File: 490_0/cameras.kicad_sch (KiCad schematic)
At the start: 2 parts, among them J1 2 lane camera interface, J2 4 lane camera interface

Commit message: Update cameras.kicad_sch
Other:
- note added: "WIDE ANGLE VERSION Horizontal field of view: 102 degrees Vertical field of view: 67 degrees"

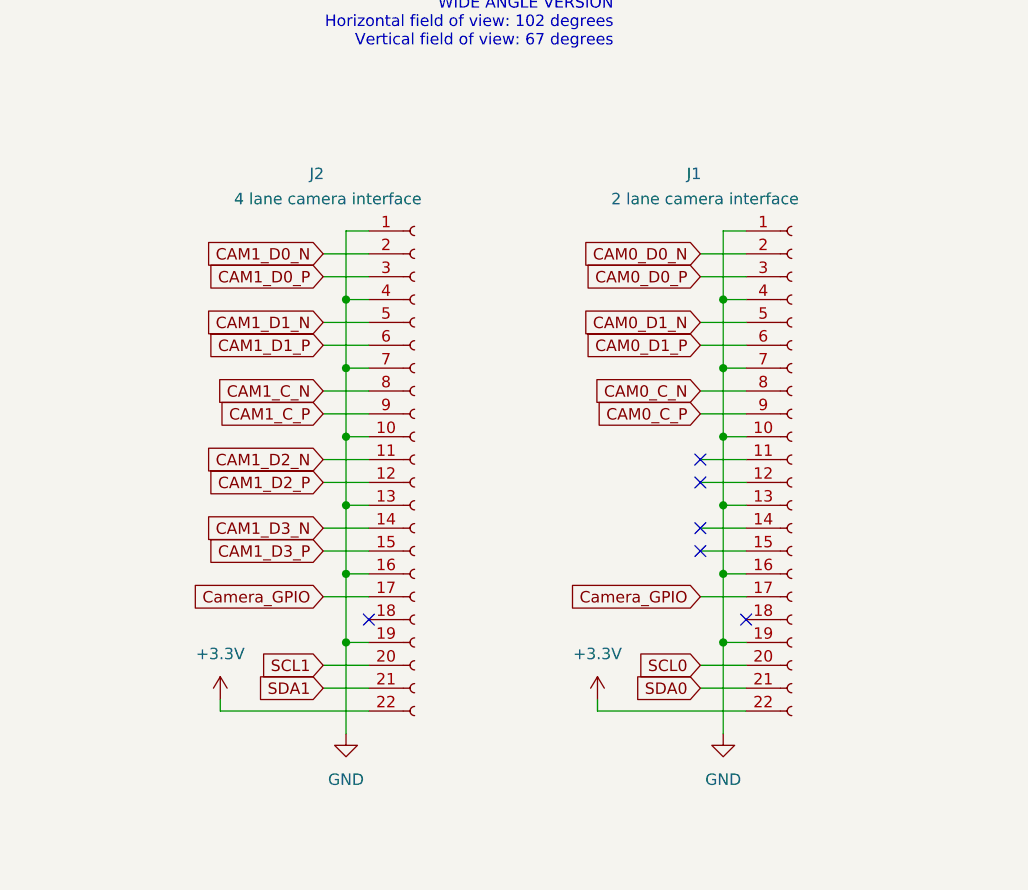
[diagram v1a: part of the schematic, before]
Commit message: Minor updates + USB 2.0
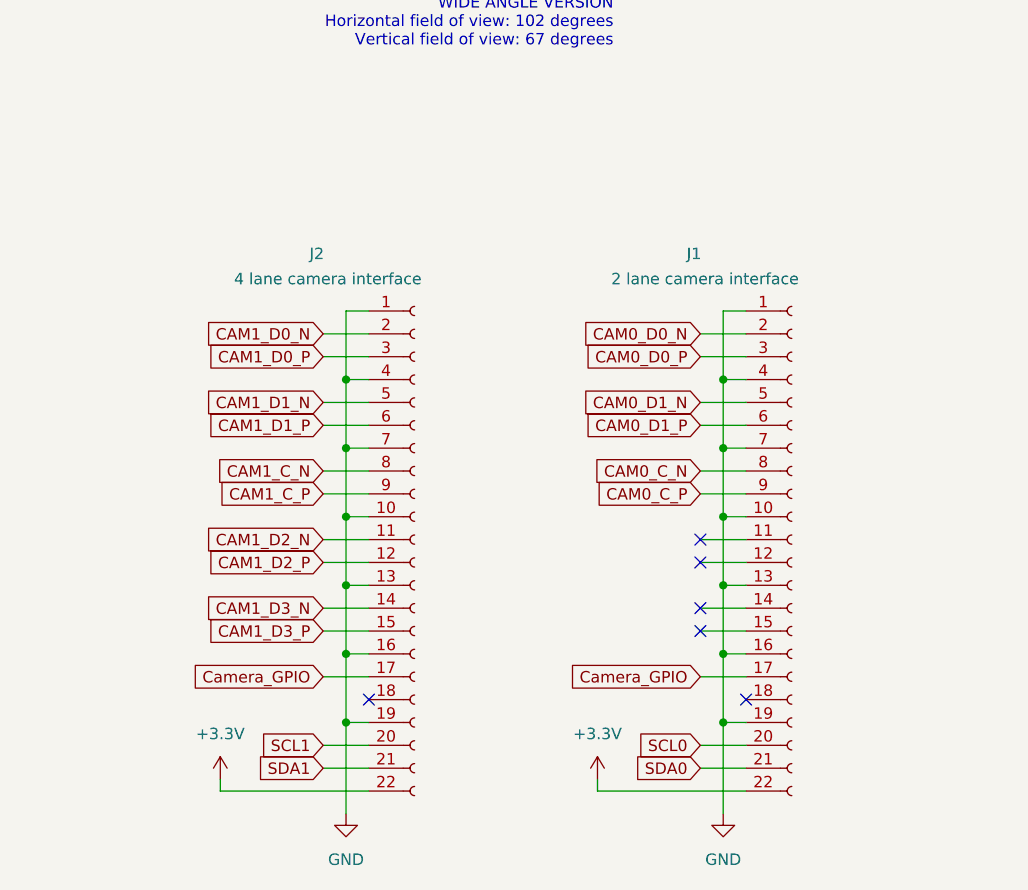
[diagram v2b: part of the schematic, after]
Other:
- moved on the sheet: J1, J2

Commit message: Minor updates
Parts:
- added J5: Conn_01x15_FPC_0.5mm, PCM_SparkFun-Connector:FPC_1x16_P0.5mm_Horizontal_DualContact, symbol PCM_SparkFun-Connector:Conn_01x16_FPC_P0.5mm_Horizontal_DualContact
- J7: renamed from J1; now not fitted
- renumbered J2 to J6
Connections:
- net +3.3V: now also J5.15 (Pin_15)
- net CAM0_C_N: now also J5.8 (Pin_8)
- net CAM0_C_P: now also J5.9 (Pin_9)
- net CAM0_D0_N: now also J5.2 (Pin_2)
- net CAM0_D0_P: now also J5.3 (Pin_3)
- net CAM0_D1_N: now also J5.5 (Pin_5)
- net CAM0_D1_P: now also J5.6 (Pin_6)
- net Camera_GPIO: now also J5.11 (Pin_11)
- net GND: now also J5.1 (Pin_1), J5.10 (Pin_10), J5.4 (Pin_4), J5.7 (Pin_7)
- net SCL0: now also J5.13 (Pin_13)
- net SDA0: now also J5.14 (Pin_14)
- no-connect marks 6 -> 7

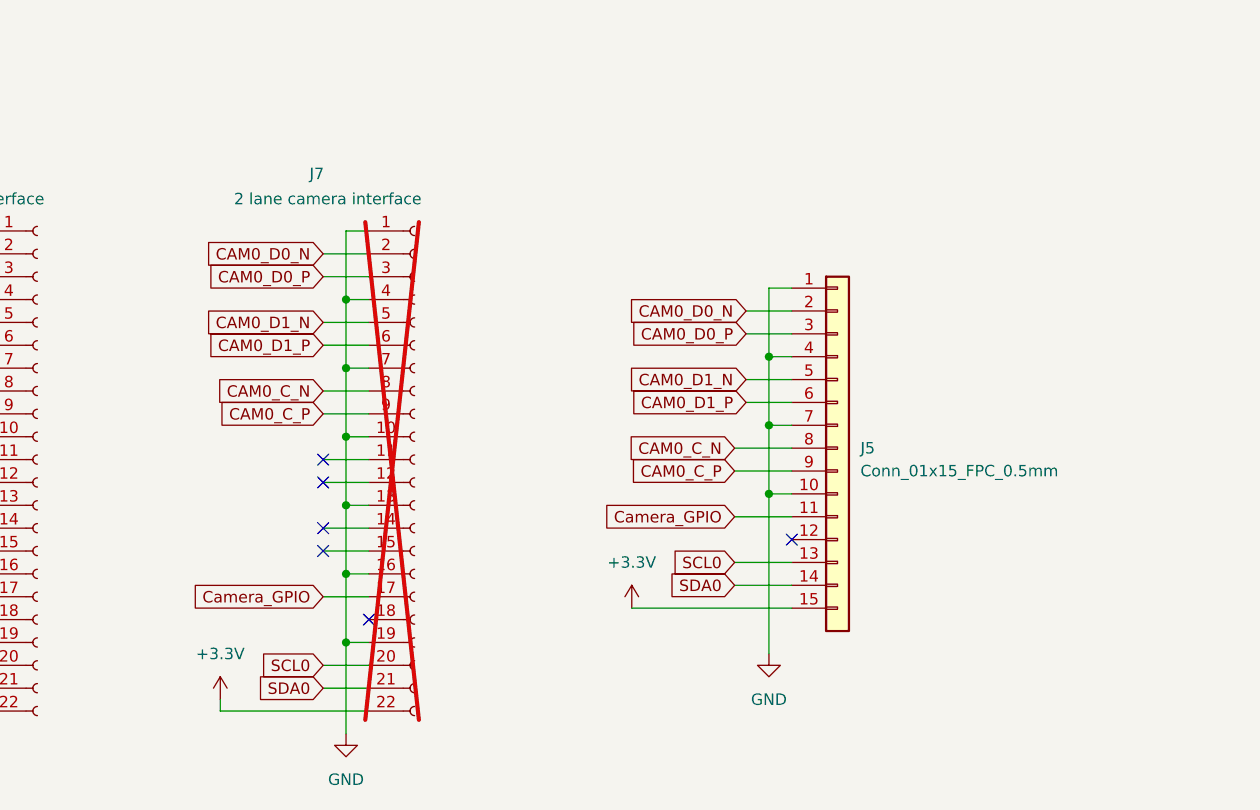
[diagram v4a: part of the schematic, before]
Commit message: Updated block diagram
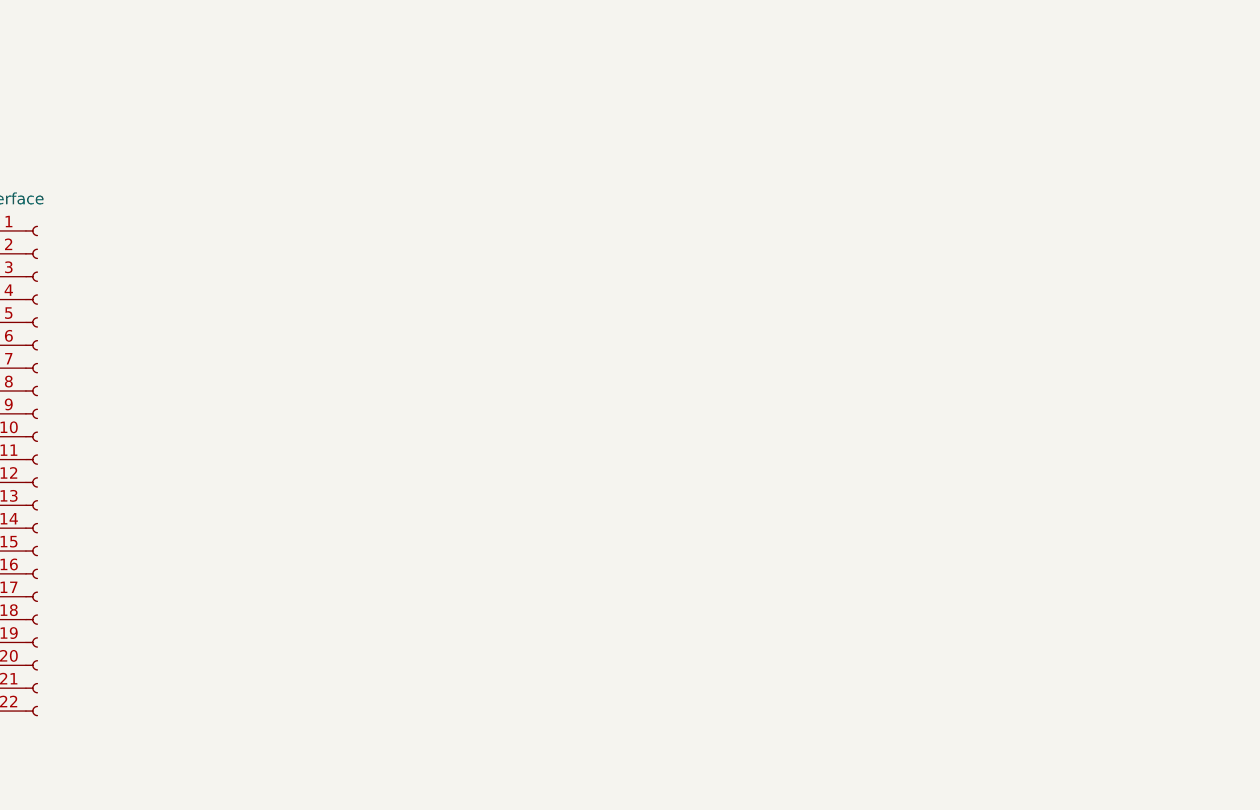
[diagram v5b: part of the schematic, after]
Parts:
- removed J5: Conn_01x15_FPC_0.5mm, PCM_SparkFun-Connector:FPC_1x16_P0.5mm_Horizontal_DualContact, symbol PCM_SparkFun-Connector:Conn_01x16_FPC_P0.5mm_Horizontal_DualContact
- removed J7: 2 lane camera interface, symbol Connector:Conn_01x22_Socket
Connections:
- no-connect marks 7 -> 1

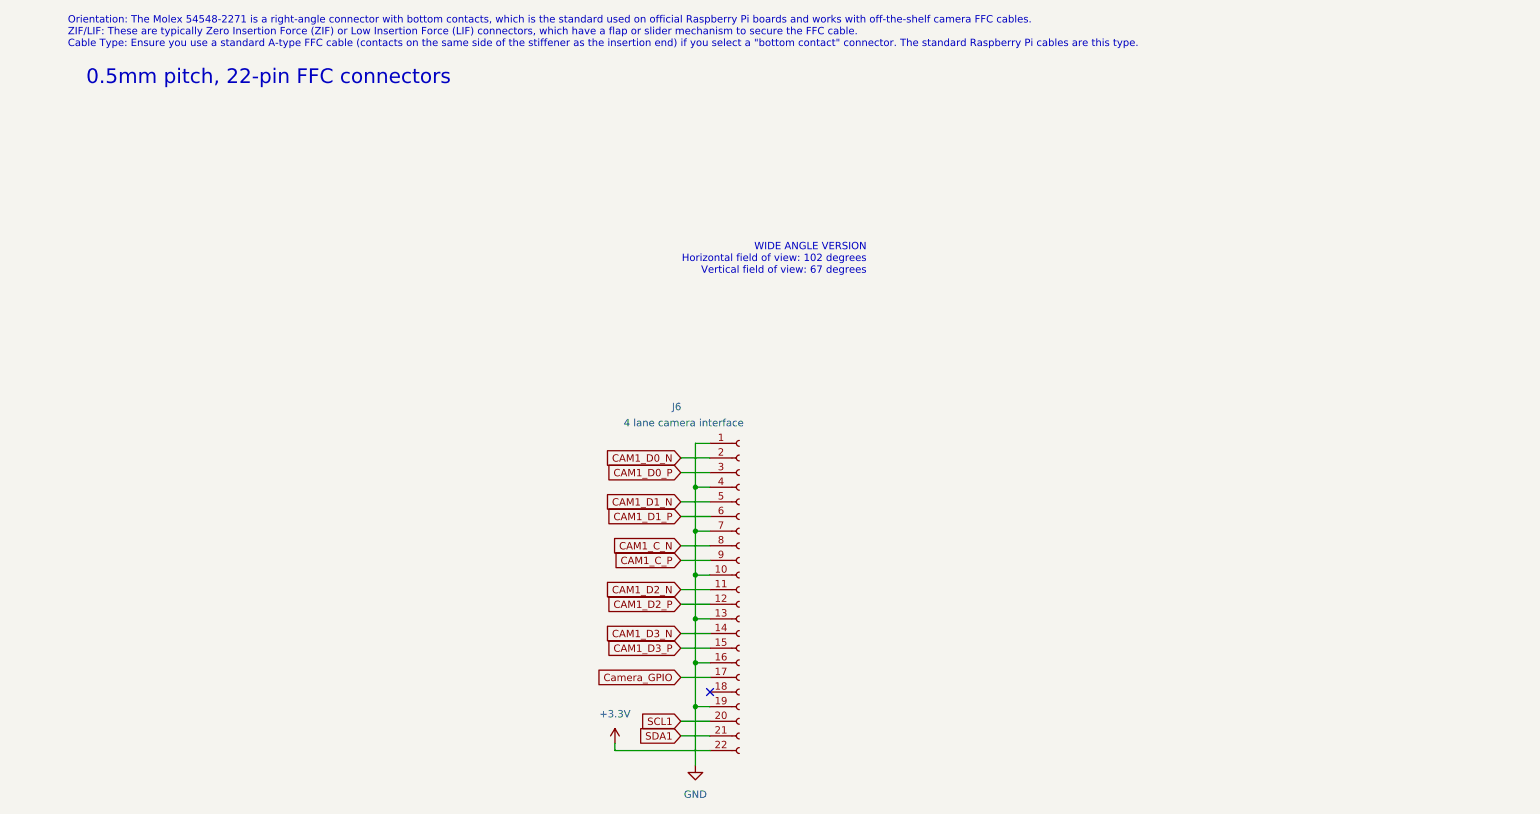
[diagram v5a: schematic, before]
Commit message: changed PCB block diagram
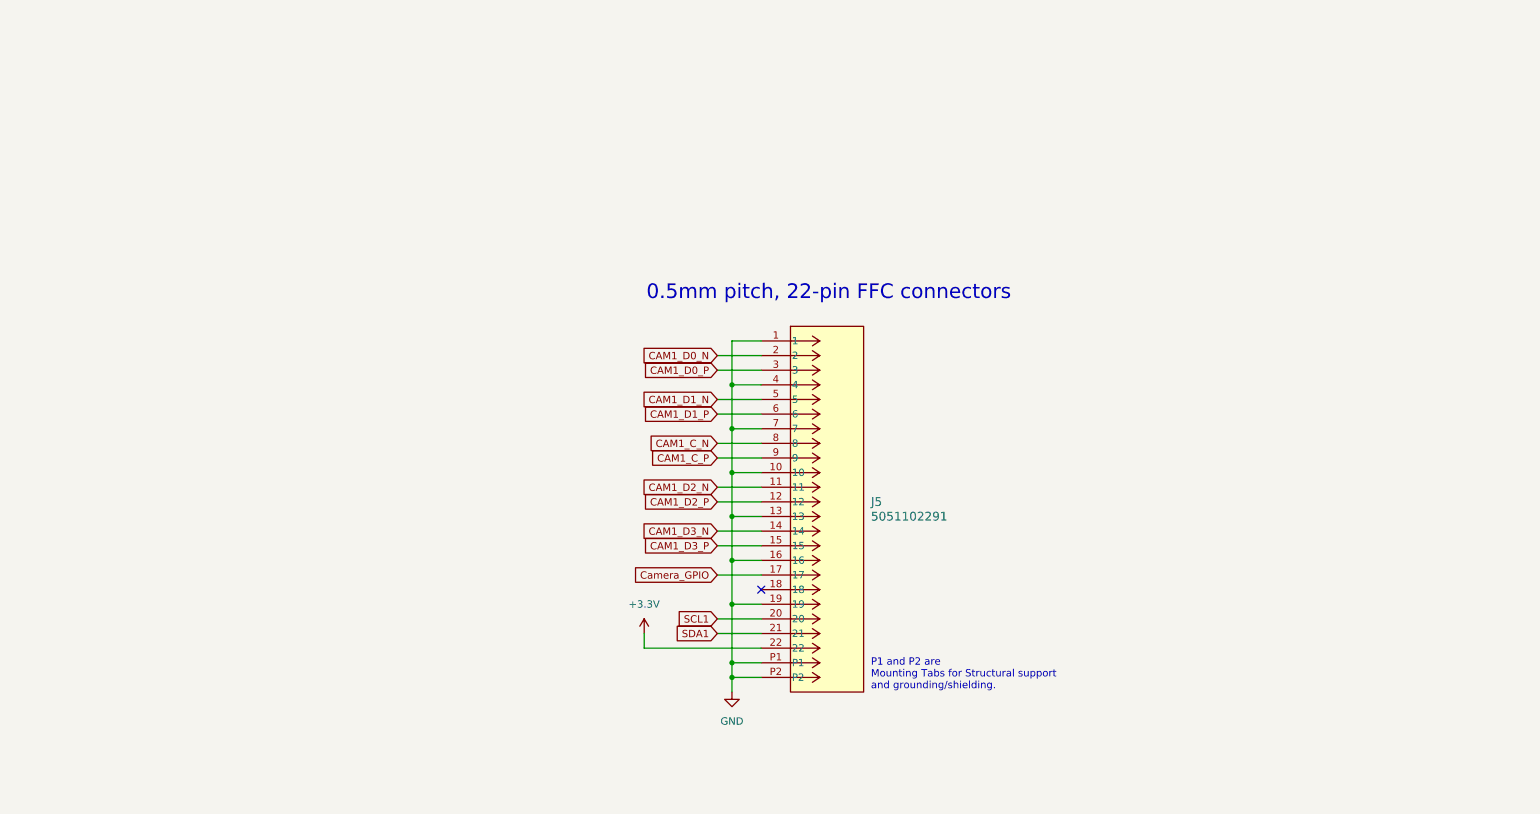
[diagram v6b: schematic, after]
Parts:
- removed J6: 4 lane camera interface, symbol Connector:Conn_01x22_Socket
- added J5: 5051102291, CON_5051102291_MOL, symbol capstone_parts:5051102291
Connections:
- net +3.3V: now also J5.22
- net CAM1_C_N: now also J5.8
- net CAM1_C_P: now also J5.9
- net CAM1_D0_N: now also J5.2
- net CAM1_D0_P: now also J5.3
- net CAM1_D1_N: now also J5.5
- net CAM1_D1_P: now also J5.6
- net CAM1_D2_N: now also J5.11
- net CAM1_D2_P: now also J5.12
- net CAM1_D3_N: now also J5.14
- net CAM1_D3_P: now also J5.15
- net Camera_GPIO: now also J5.17
- net GND: now also J5.1, J5.10, J5.13, J5.16, J5.19, J5.4, J5.7, J5.P1, J5.P2
- net SCL1: now also J5.20
- net SDA1: now also J5.21
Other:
- note added: "P1 and P2 are Mounting Tabs for Structural support and grounding/shielding."
- note removed: "Orientation: The Molex 54548-2271 is a right-angle connector with bottom contacts, which is the standard used on official Raspberry Pi boards and works with off-the-shelf camera FFC cables. ZIF/LIF: These are typically Zero Insertion Force (ZIF) or Low Insertion Force (LIF) connectors, which have a flap or slider mechanism to secure the FFC cable. Cable Type: Ensure you use a standard A-type FFC 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"
- note removed: "WIDE ANGLE VERSION Horizontal field of view: 102 degrees Vertical field of view: 67 degrees"
